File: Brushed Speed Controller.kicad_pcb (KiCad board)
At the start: 2 copper layers, 6 parts, among them Q1 ISC037N03L5ISATMA1, Q2 ISC037N03L5ISATMA1, Q3 BSC340N08NS3, Q4 BSC340N08NS3, U1 TC4427, U2 TC4427

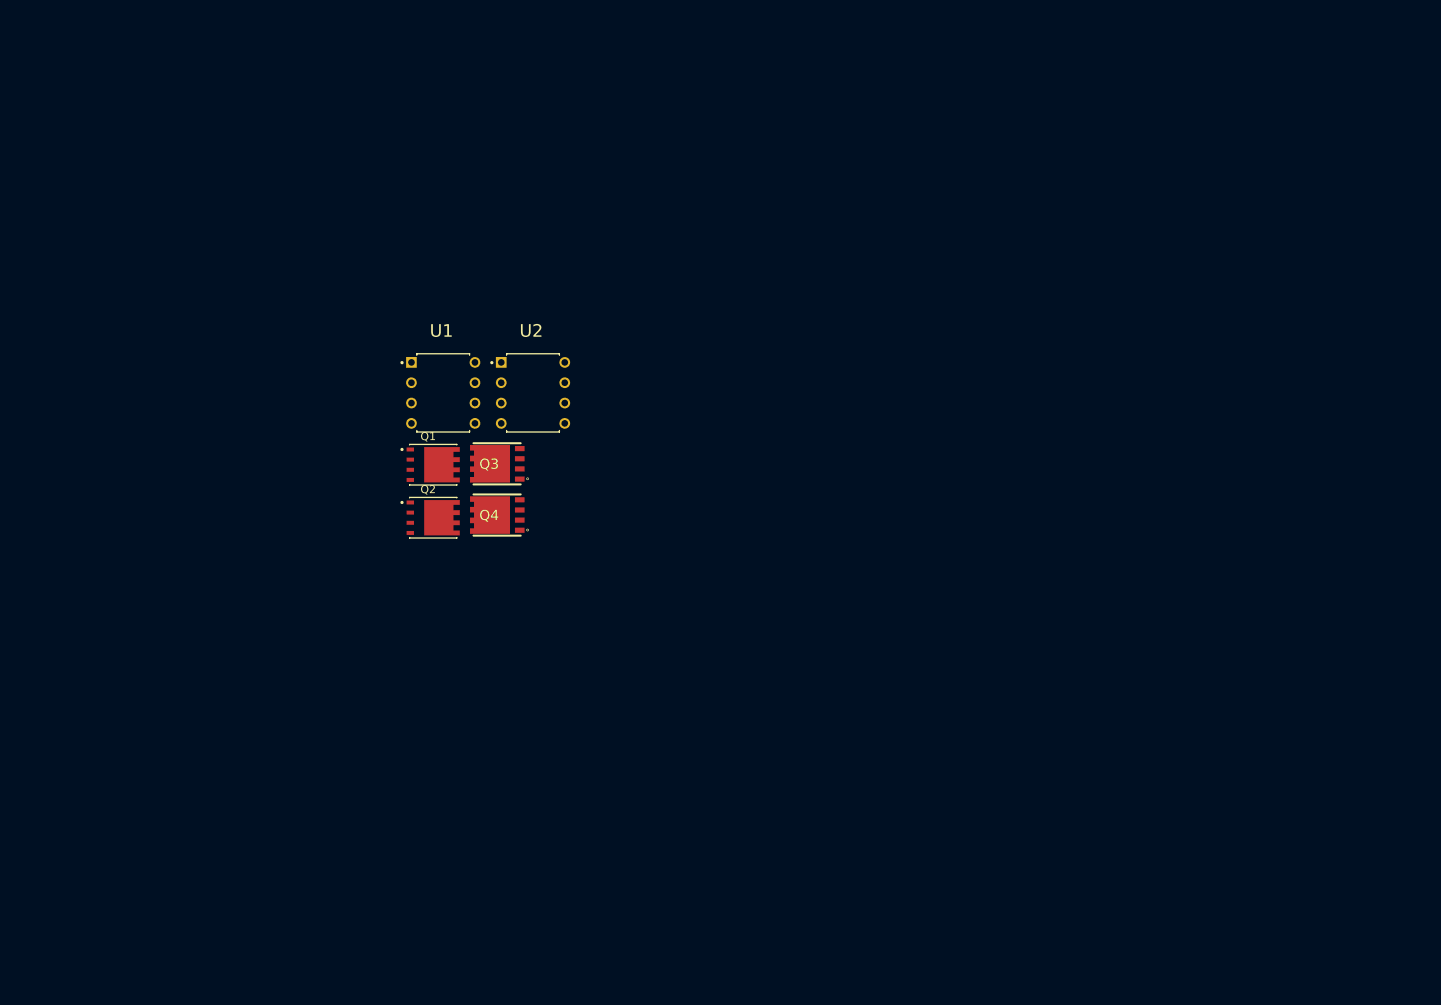
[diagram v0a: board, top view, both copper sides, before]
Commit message: Made first prototype PCB
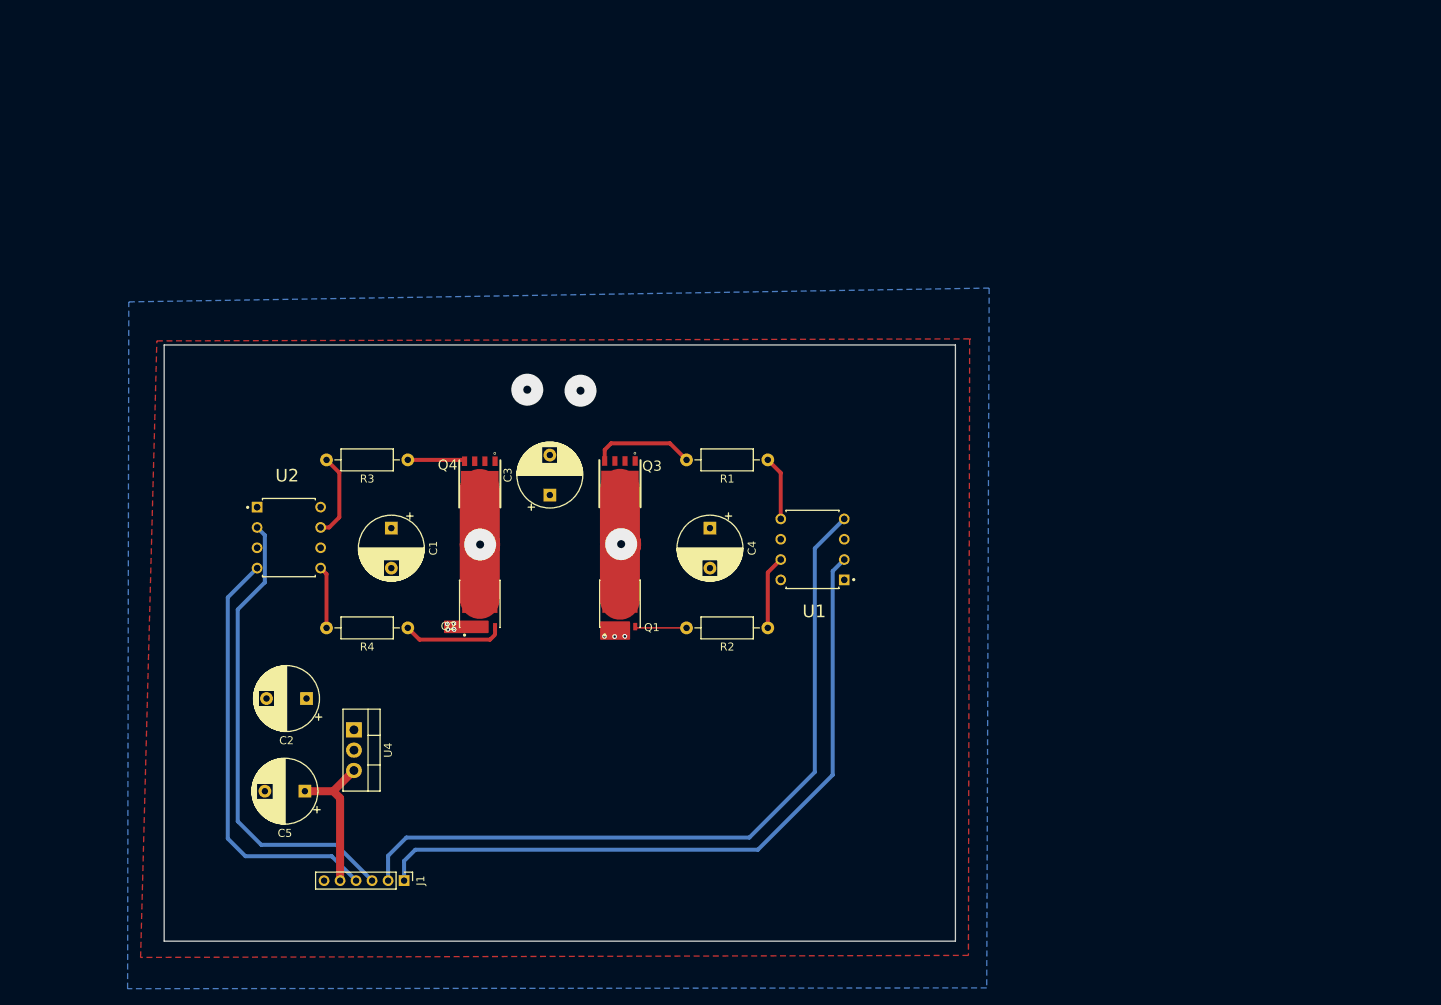
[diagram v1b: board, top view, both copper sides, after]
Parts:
- added C1: C_Polarized, Capacitor_THT:CP_Radial_D8.0mm_P5.00mm, F.Cu at (78.9, 85.5)
- added C2: C, Capacitor_THT:CP_Radial_D8.0mm_P5.00mm, F.Cu at (68.3, 106.8)
- added C3: C, Capacitor_THT:CP_Radial_D8.0mm_P5.00mm, F.Cu at (98.8, 81.4)
- added C4: C, Capacitor_THT:CP_Radial_D8.0mm_P5.00mm, F.Cu at (118.8, 85.5)
- added C5: C, Capacitor_THT:CP_Radial_D8.0mm_P5.00mm, F.Cu at (68.1, 118.4)
- added J1: Conn_01x06_Pin, Connector_PinHeader_2.00mm:PinHeader_1x06_P2.00mm_Vertical, F.Cu at (80.5, 129.6)
- added R1: R, Resistor_THT:R_Axial_DIN0207_L6.3mm_D2.5mm_P10.16mm_Horizontal, F.Cu at (126.0, 77.0)
- added R2: R, Resistor_THT:R_Axial_DIN0207_L6.3mm_D2.5mm_P10.16mm_Horizontal, F.Cu at (126.0, 98.0)
- added R3: R, Resistor_THT:R_Axial_DIN0207_L6.3mm_D2.5mm_P10.16mm_Horizontal, F.Cu at (81.0, 77.0)
- added R4: R, Resistor_THT:R_Axial_DIN0207_L6.3mm_D2.5mm_P10.16mm_Horizontal, F.Cu at (81.0, 98.0)
- added U4: L7805, Package_TO_SOT_THT:TO-220-3_Vertical, F.Cu at (74.3, 110.7)
- moved U1 50.1 mm to (131.6, 88.2), turned to 180 degrees
- moved U2 35.5 mm to (66.1, 86.7)
- moved Q1 29.1 mm to (107.5, 95.0), turned to 90 degrees
- moved Q3 15.6 mm to (107.5, 80.0), turned to 90 degrees
- moved Q2 12.2 mm to (90.0, 95.0), turned to 90 degrees
- moved Q4 4.46 mm to (90.0, 80.0), turned to 90 degrees
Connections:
- Q1 pad 2: (no net) -> GND
- Q1 pad 3: (no net) -> GND
- Q2 pad 2: (no net) -> GND
- Q2 pad 3: (no net) -> GND
- Q3 pad 9: (no net) -> Net-(Q3-D_1)
- Q4 pad 9: (no net) -> Net-(Q4-D_1)
- U1 pad 2: unconnected-(U1-IN_A-Pad2) -> /IN1
- U1 pad 4: unconnected-(U1-IN_B-Pad4) -> /IN2
- U2 pad 2: Net-(U2-IN_A) -> /IN3
- U2 pad 3: unconnected-(U2-GND-Pad3) -> GND
- U2 pad 4: Net-(U2-IN_B) -> /IN4
- U2 pad 5: unconnected-(U2-~{OUT_B}-Pad5) -> Net-(U2-~{OUT_B})
- U2 pad 6: unconnected-(U2-VDD-Pad6) -> VCC
- U2 pad 7: unconnected-(U2-~{OUT_A}-Pad7) -> Net-(U2-~{OUT_A})
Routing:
- net /IN2: track 0.00 -> 93.9 mm
- net /IN1: track 0.00 -> 88.0 mm
- net /IN3: track 0.00 -> 58.4 mm
- net /IN4: track 0.00 -> 53.5 mm
- net +5V: track 0.00 -> 18.7 mm
- net Net-(Q3-D_1): track 0.00 -> 14.0 mm, vias 0 -> 1
- net Net-(Q4-D_1): track 0.00 -> 13.8 mm, vias 0 -> 1
- net Net-(Q3-G): track 0.00 -> 12.8 mm
- net Net-(Q2-Pad4): track 0.00 -> 12.8 mm
- net Net-(U2-~{OUT_A}): track 0.00 -> 10.7 mm
- net Net-(U1-~{OUT_A}): track 0.00 -> 9.21 mm
- net Net-(U1-~{OUT_B}): track 0.00 -> 8.05 mm
- net Net-(U2-~{OUT_B}): track 0.00 -> 7.78 mm
- net Net-(Q4-G): track 0.00 -> 7.16 mm
- net Net-(Q1-Pad4): track 0.00 -> 6.48 mm
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- added copper zone on B.Cu, net GND
- added copper zone on F.Cu, net VCC
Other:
- board outline added: 98.9 x 74.5 mm

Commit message: made symbol for mosfet
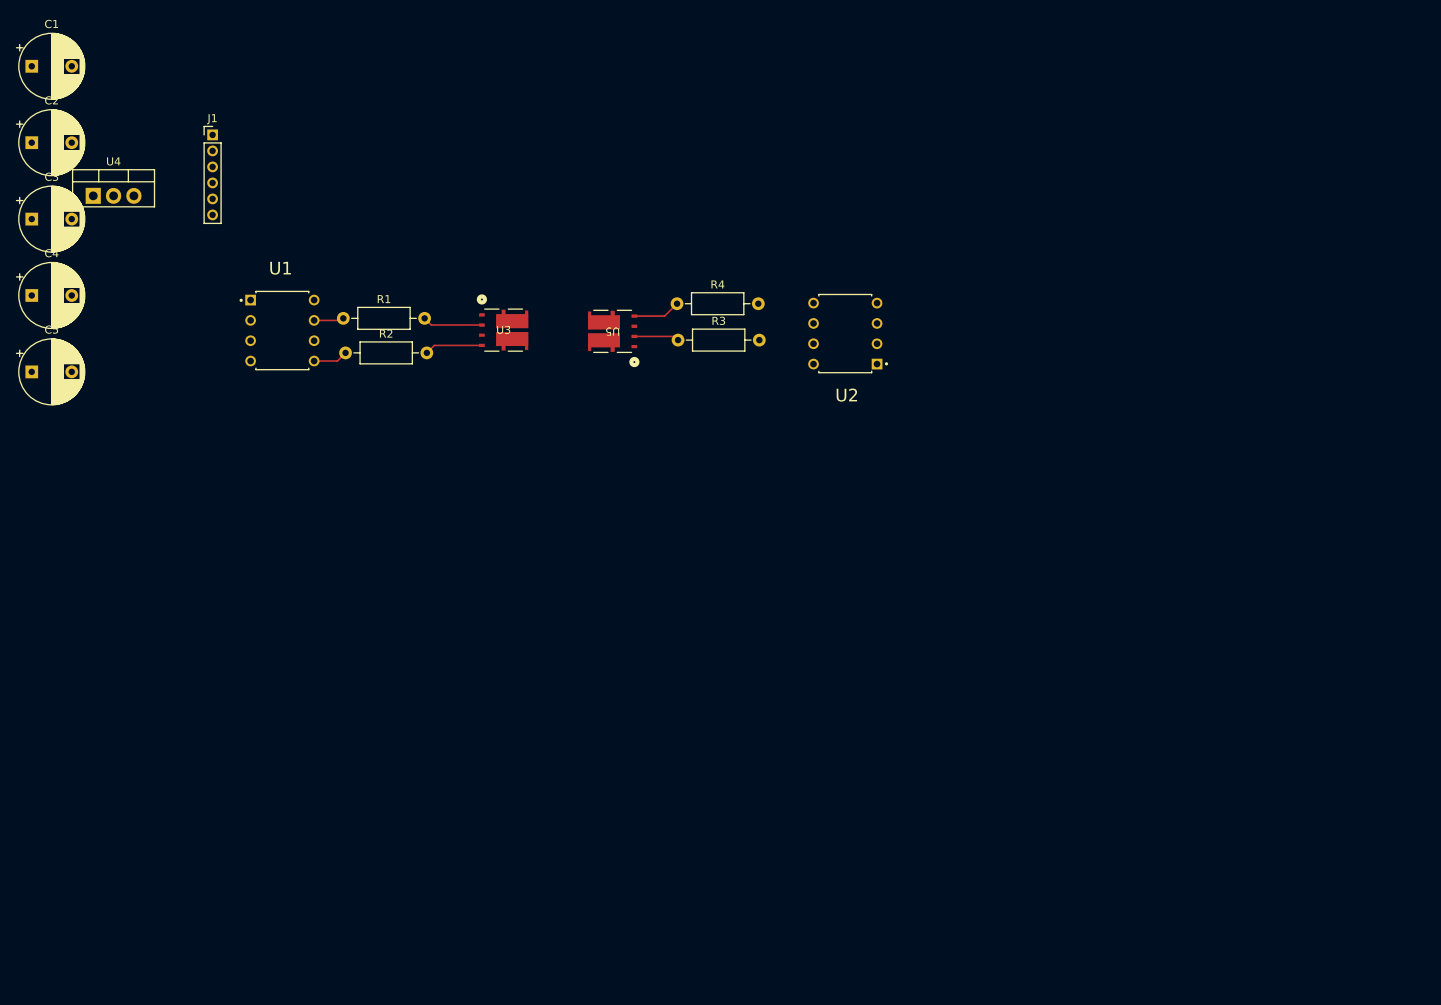
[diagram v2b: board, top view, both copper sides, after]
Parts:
- removed Q1, Q2: ISC037N03L5ISATMA1, ISC037N03:IC_ISC037N03L5ISATMA1
- removed Q3, Q4: BSC340N08NS3, BSC340N08:BSC340N08NS3
- added U3: SQJ500AEP-T1_GE3, SQJ500AEP-T1-GE3:SQJ500AEP-T1-GE3, F.Cu at (93.0, 60.8)
- added U5: SQJ500AEP-T1_GE3, SQJ500AEP-T1-GE3:SQJ500AEP-T1-GE3, F.Cu at (106.6, 60.9)
- moved J1 96.2 mm to (56.6, 36.4), turned to 0 degrees
- moved C4 89.6 mm to (34.0, 56.4), turned to 0 degrees
- moved C2 77.5 mm to (34.0, 37.3), turned to 0 degrees
- moved U4 74.3 mm to (41.7, 44.0), turned to 0 degrees
- moved U2 74.1 mm to (135.7, 61.2), turned to 180 degrees
- moved C3 73.4 mm to (34.0, 46.9), turned to 0 degrees
- moved C1 73.2 mm to (34.0, 27.8), turned to 0 degrees
- moved U1 71.7 mm to (65.3, 60.8), turned to 0 degrees
- moved R2 63.0 mm to (73.2, 63.6), turned to 0 degrees
- moved C5 62.6 mm to (34.0, 66.0), turned to 0 degrees
- moved R1 55.9 mm to (72.9, 59.3), turned to 0 degrees
- moved R4 52.7 mm to (114.7, 57.5), turned to 0 degrees
- moved R3 37.0 mm to (114.8, 62.0), turned to 0 degrees
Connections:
- R1 pad 1: Net-(U1-~{OUT_B}) -> Net-(U1-~{OUT_A})
- R2 pad 1: Net-(U1-~{OUT_A}) -> Net-(U1-~{OUT_B})
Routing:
- net /IN2: track 93.9 -> 0.00 mm
- net /IN1: track 88.0 -> 0.00 mm
- net /IN3: track 58.4 -> 0.00 mm
- net /IN4: track 53.5 -> 0.00 mm
- net +5V: track 18.7 -> 0.00 mm
- net Net-(Q3-D_1): track 14.0 -> 0.00 mm, vias 1 -> 0
- net Net-(Q4-D_1): track 13.8 -> 0.00 mm, vias 1 -> 0
- net Net-(U2-~{OUT_A}): track 10.7 -> 0.00 mm
- net Net-(U2-~{OUT_B}): track 7.78 -> 0.00 mm
- net Net-(U5-G2): track 12.8 -> 5.98 mm
- net Net-(U1-~{OUT_A}): track 9.21 -> 3.76 mm
- net Net-(U3-G1): track 12.8 -> 7.51 mm
- net Net-(U1-~{OUT_B}): track 8.05 -> 4.35 mm
- net Net-(U5-G1): track 7.16 -> 5.65 mm
- net Net-(U3-G2): track 6.48 -> 7.27 mm
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- removed copper zone on B.Cu, net GND
- removed copper zone on F.Cu, net VCC
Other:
- board outline removed

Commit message: Completed the PCB and Schemetic
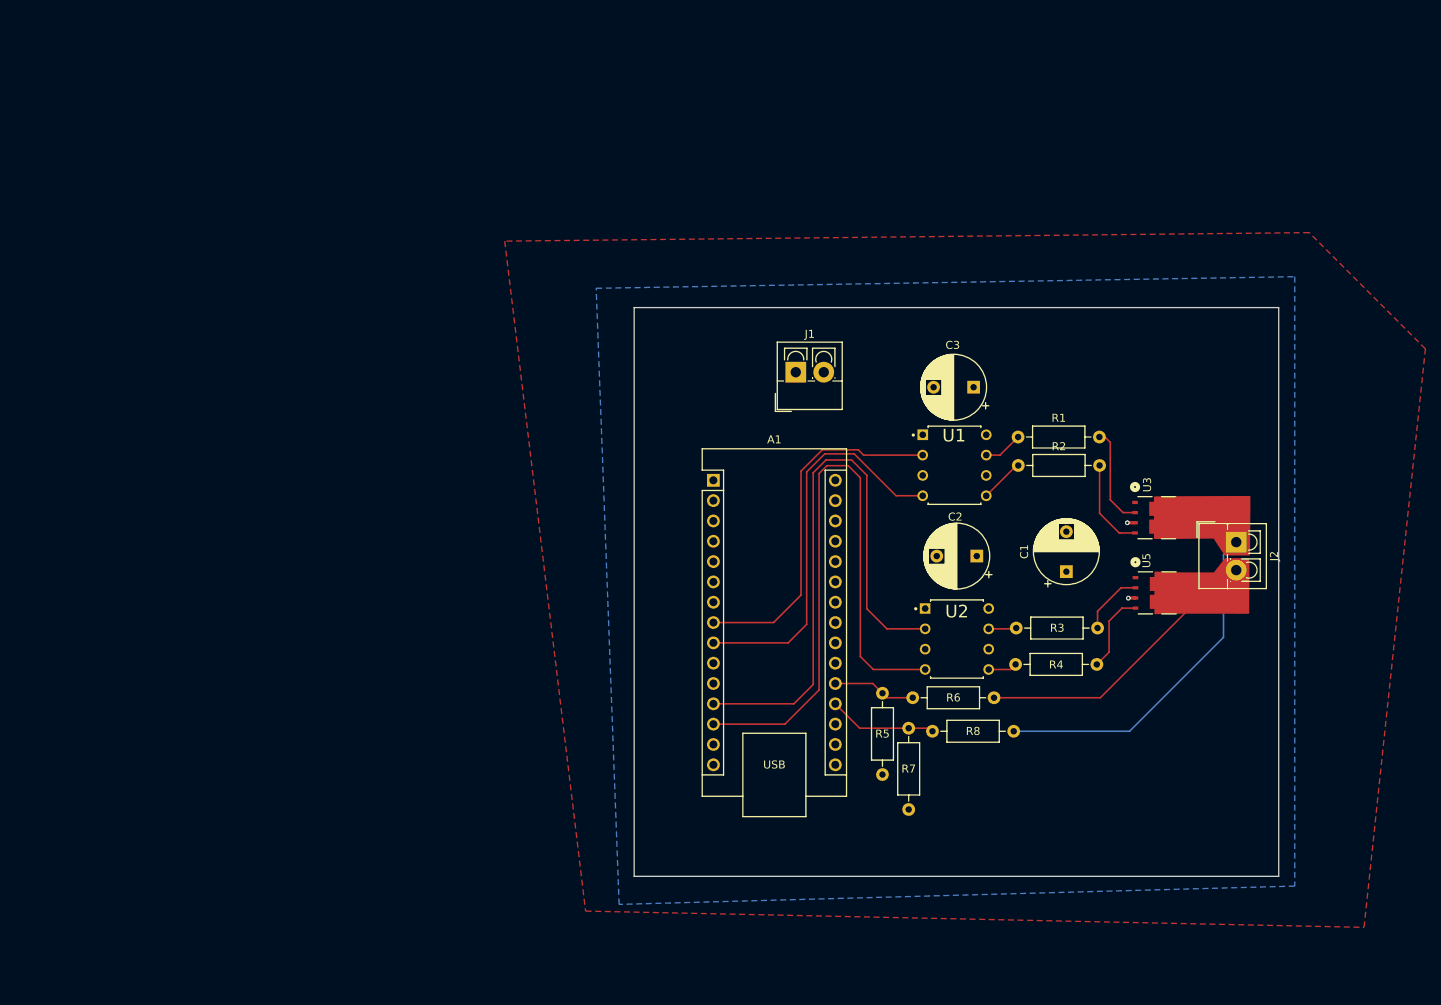
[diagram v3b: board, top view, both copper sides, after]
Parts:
- removed C4, C5: C, Capacitor_THT:CP_Radial_D8.0mm_P5.00mm
- removed U4: L7805, Package_TO_SOT_THT:TO-220-3_Vertical
- added A1: Arduino_Nano_v3.x, Module:Arduino_Nano, F.Cu at (119.2, 79.6)
- added J2: Output, TerminalBlock_4Ucon:TerminalBlock_4Ucon_1x02_P3.50mm_Vertical, F.Cu at (184.6, 87.3)
- added R5: R, Resistor_THT:R_Axial_DIN0207_L6.3mm_D2.5mm_P10.16mm_Horizontal, F.Cu at (140.3, 116.3)
- added R6: R, Resistor_THT:R_Axial_DIN0207_L6.3mm_D2.5mm_P10.16mm_Horizontal, F.Cu at (144.1, 106.7)
- added R7: R, Resistor_THT:R_Axial_DIN0207_L6.3mm_D2.5mm_P10.16mm_Horizontal, F.Cu at (143.6, 120.7)
- added R8: R, Resistor_THT:R_Axial_DIN0207_L6.3mm_D2.5mm_P10.16mm_Horizontal, F.Cu at (146.6, 110.9)
- J1: value Conn_01x06_Pin -> Input; footprint Connector_PinHeader_2.00mm:PinHeader_1x06_P2.00mm_Vertical -> TerminalBlock_4Ucon:TerminalBlock_4Ucon_1x02_P3.50mm_Vertical
- moved C1 143.9 mm to (163.3, 91.0), turned to 90 degrees
- moved C2 128.9 mm to (152.1, 89.0), turned to 180 degrees
- moved C3 119.6 mm to (151.7, 67.9), turned to 180 degrees
- moved U1 85.7 mm to (149.3, 77.7)
- moved R1 85.6 mm to (157.3, 74.1)
- moved R2 85.3 mm to (157.3, 77.7)
- moved U3 84.9 mm to (174.6, 84.2)
- moved J1 78.7 mm to (129.5, 66.0)
- moved U5 75.5 mm to (174.7, 93.6), turned to 0 degrees
- moved R4 69.2 mm to (167.1, 102.6), turned to 180 degrees
- moved R3 63.6 mm to (167.2, 98.0), turned to 180 degrees
- moved U2 40.6 mm to (149.6, 99.4), turned to 0 degrees
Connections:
- net Net-(U3-D1) renamed /OUT1
- net Net-(U3-G1) renamed /VG1
- net Net-(U3-G2) renamed /VG2
- net Net-(U5-D1) renamed /OUT2
- net Net-(U5-G1) renamed /VG3
- net Net-(U5-G2) renamed /VG4
- J1 pad 1: /IN1 -> VCC
- J1 pad 2: /IN2 -> GND
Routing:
- net /IN4: track 0.00 -> 79.3 mm
- net /IN3: track 0.00 -> 73.1 mm
- net /IN2: track 0.00 -> 49.3 mm
- net /IN1: track 0.00 -> 44.5 mm
- net /OUT1: track 0.00 -> 43.6 mm
- net /OUT2: track 0.00 -> 32.5 mm
- net Net-(A1-A0): track 0.00 -> 13.6 mm
- net Net-(A1-A1): track 0.00 -> 10.4 mm
- net /VG1: track 7.51 -> 12.6 mm
- net /VG2: track 7.27 -> 11.5 mm
- net /VG4: track 5.98 -> 10.0 mm
- net Net-(U2-~{OUT_B}): track 0.00 -> 3.62 mm
- net Net-(U2-~{OUT_A}): track 0.00 -> 3.49 mm
- net /VG3: track 5.65 -> 8.05 mm
- net GND: track 0.00 -> 1.89 mm, vias 0 -> 2
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- added copper zone on B.Cu, net GND
- added copper zone on F.Cu, net VCC
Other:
- board outline added: 80.6 x 71.1 mm

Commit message: Added L7805 to PCB
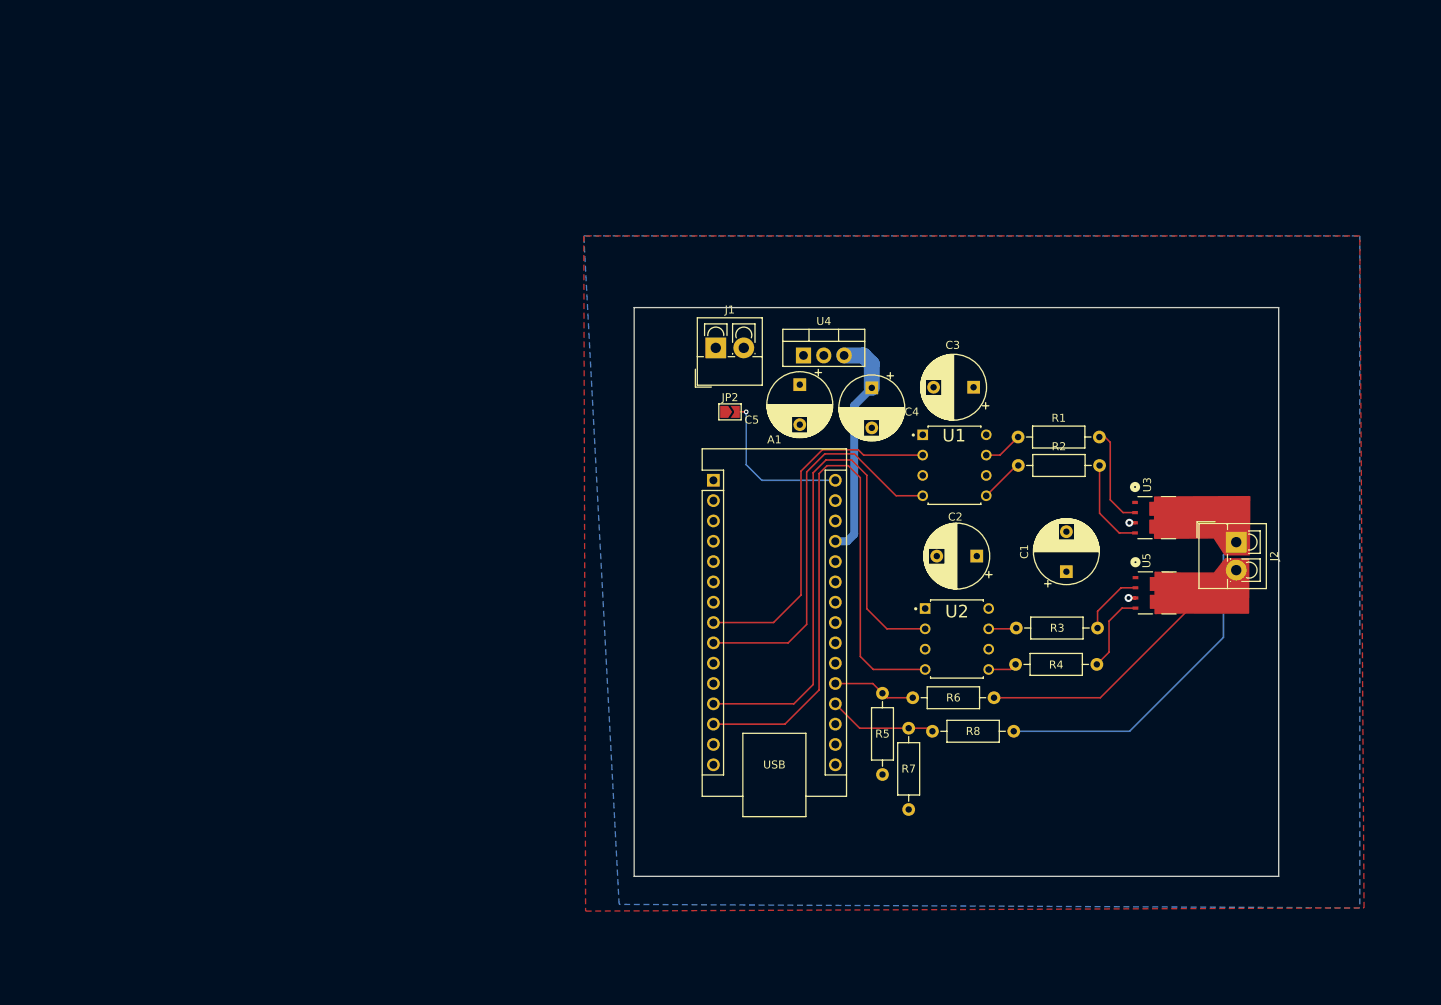
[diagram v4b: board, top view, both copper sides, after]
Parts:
- added C4: C, Capacitor_THT:CP_Radial_D8.0mm_P5.00mm, F.Cu at (139.0, 68.0)
- added C5: C, Capacitor_THT:CP_Radial_D8.0mm_P5.00mm, F.Cu at (130.0, 67.6)
- added JP2: SolderJumper, Jumper:SolderJumper-2_P1.3mm_Open_TrianglePad1.0x1.5mm, F.Cu at (121.3, 71.0)
- added U4: LM7805, Package_TO_SOT_THT:TO-220-3_Vertical, F.Cu at (130.5, 63.9)
- moved J1 10.4 mm to (119.5, 63.0)
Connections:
- A1 pad 30: VCC -> Net-(A1-VIN)
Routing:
- net +5V: track 0.00 -> 28.8 mm
- net Net-(A1-VIN): track 0.00 -> 19.9 mm, vias 0 -> 1
